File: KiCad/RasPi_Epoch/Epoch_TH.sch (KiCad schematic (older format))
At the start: 21 parts, among them P1 RasPi_GPIO, P2 CONN_1, P3 CONN_1, P4 CONN_1, P5 32k, P6 CONN_1, P7 CONN_1, P8 CONN_1, P9 SQW, U1 DS3231N, U2 DS1307, X1 CRYSTAL

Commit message: Epoch_smd looks done (all parts on lower side). Epoch_TH in progress.
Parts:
- removed C1: 100n, cnp_3mm_disc, symbol C
- removed P2, P3, P4: CONN_1, Pad01, symbol CONN_1
- removed P5: 32k, symbol CONN_2
- removed R4, R5: 4k7, rc03_vert, symbol R
- removed U1: DS3231N, DS3231, symbol DS3231N
- P9: footprint (none) -> ShortLink3
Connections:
- net labels removed: 32k, RST, Rpi_32k
- wire segments 78 -> 47
- no-connect marks 22 -> 23
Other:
- note removed: "Breakout Pads"
- moved on the sheet: R1, R2, R3

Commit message: RasPi_Epoch : Epoch_TH done. Need to verify the circuit and layout.
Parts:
- removed R1, R2, R3: 4k7, rc03_vert, symbol R
- added P2: I/O, Pad01, symbol I/O
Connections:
- wire segments 47 -> 41
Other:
- note added: "DS1307 (Optional)\nVcc is tied to 5V0 on Ras-Pi, but SCL and SDA are forced to 3V3\nsince no pull up resistors are used.\nNeed to verify if this works."
- note removed: "DS1307 (Optional)\nVcc is tied to 5V0 on Ras-Pi, but SCL and SDA are pulled up to 3V3.\nNeed to verify if this works."
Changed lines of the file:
@@
-EESchema Schematic File Version 2  date Friday 15 March 2013 09:54:40 PM IST
+EESchema Schematic File Version 2  date Friday 15 March 2013 10:32:39 PM IST
 LIBS:RasPi_RTC
 LIBS:RasPi_RTC2
@@
 Comment4 ""
 $EndDescr
+Wire Wire Line
+	4000 5650 5475 5650
+Wire Wire Line
+	5475 5650 5475 5550
+Wire Notes Line
+	1025 7000 1025 3675
+Wire Notes Line
+	1025 7000 5850 7000
+Wire Notes Line
+	5850 7000 5850 3675
+Wire Notes Line
+	5850 3675 1025 3675
+Wire Wire Line
+	3150 1900 3675 1900
+Wire Wire Line
+	5925 3000 5425 3000
+Wire Wire Line
+	5425 3000 5425 2900
+Wire Wire Line
+	1850 3000 1150 3000
+Wire Wire Line
+	3150 2100 3800 2100
+Wire Wire Line
+	3800 2100 3800 1025
+Connection ~ 1725 6150
+Wire Wire Line
+	1725 6200 1725 4500
+Connection ~ 2100 4700
+Wire Wire Line
+	2100 6200 2100 4700
+Connection ~ 2350 6700
+Wire Wire Line
+	2350 6700 2350 6600
+Connection ~ 1725 4700
+Connection ~ 2500 6700
+Wire Wire Line
+	2500 6700 2500 5550
+Wire Wire Line
+	4950 5250 4000 5250
+Wire Wire Line
+	2500 5550 2650 5550
+Wire Wire Line
+	2800 5900 2950 5900
+Wire Wire Line
+	2800 5900 2800 5750
+Wire Wire Line
+	2800 5350 2800 5200
+Wire Wire Line
+	3100 5850 3025 5850
+Wire Wire Line
+	4075 5850 4075 4700
+Wire Wire Line
+	4075 5850 4000 5850
+Wire Wire Line
+	3025 5850 3025 6825
+Wire Wire Line
+	3100 5250 3025 5250
+Connection ~ 3025 6700
+Wire Wire Line
+	3025 5250 3025 4475
+Connection ~ 3025 4575
+Wire Wire Line
+	4000 5450 4950 5450
+Wire Wire Line
+	4075 4700 1725 4700
+Wire Wire Line
+	2950 5450 2950 5200
+Wire Wire Line
+	2950 5450 3100 5450
+Wire Wire Line
+	3100 5650 2950 5650
+Wire Wire Line
+	2950 5650 2950 5900
+Wire Wire Line
+	2950 5200 2800 5200
+Wire Wire Line
+	2350 6200 2350 4575
+Wire Wire Line
+	2100 6600 2100 6700
+Connection ~ 2100 6700
+Wire Wire Line
+	1725 6650 1725 6700
+Connection ~ 1600 1900
+Wire Wire Line
+	1150 2100 1850 2100
+Wire Wire Line
+	1150 2000 1850 2000
+Wire Wire Line
+	1150 1900 1850 1900
+Wire Wire Line
+	2350 4575 3025 4575
+Wire Wire Line
+	1725 6700 3025 6700
+Wire Wire Line
+	1600 1025 1600 1900
+Wire Wire Line
+	5225 2900 5225 3000
+Wire Wire Line
+	5225 3000 4750 3000
+Wire Notes Line
+	10875 3675 6100 3675
+Wire Notes Line
+	10875 3675 10875 7000
+Wire Notes Line
+	10875 7000 6100 7000
+Wire Notes Line
+	6100 7000 6100 3675
+$Comp
+L I/O P2
+U 1 1 5143534F
+P 5475 5400
+F 0 "P2" V 5525 5400 40  0000 L CNN
+F 1 "I/O" H 5475 5455 30  0001 C CNN
+F 2 "Pad01" H 5475 5400 60  0001 C CNN
+	1    5475 5400
+	0    -1   -1   0
+$EndComp
 NoConn ~ 3150 3000
-Connection ~ 4400 5650
-Wire Wire Line
-	4400 5175 4400 5650
-Wire Notes Line
-	6100 7000 6100 3675
-Wire Notes Line
-	6100 7000 10875 7000
-Wire Notes Line
-	10875 7000 10875 3675
-Wire Notes Line
-	10875 3675 6100 3675
-Connection ~ 4650 4575
-Wire Wire Line
-	4075 4575 4900 4575
-Wire Wire Line
-	4900 4575 4900 4675
-Wire Wire Line
-	4750 3000 5225 3000
-Wire Wire Line
-	5225 3000 5225 2900
-Wire Wire Line
-	1600 1025 1600 1900
-Wire Wire Line
-	3025 6700 1725 6700
-Connection ~ 4650 5450
-Wire Wire Line
-	4650 5175 4650 5450
-Wire Wire Line
-	3025 4575 2350 4575
-Wire Wire Line
-	1850 1900 1150 1900
-Wire Wire Line
-	1150 2000 1850 2000
-Wire Wire Line
-	1150 2100 1850 2100
-Connection ~ 1600 1900
-Wire Wire Line
-	1725 6700 1725 6650
-Connection ~ 2100 6700
-Wire Wire Line
-	2100 6600 2100 6700
-Wire Wire Line
-	2350 4575 2350 6200
-Wire Wire Line
-	2950 5200 2800 5200
-Wire Wire Line
-	2950 5650 2950 5900
-Wire Wire Line
-	2950 5650 3100 5650
-Wire Wire Line
-	3100 5450 2950 5450
-Wire Wire Line
-	2950 5450 2950 5200
-Wire Wire Line
-	1725 4700 4075 4700
-Wire Wire Line
-	4000 5450 5375 5450
-Connection ~ 3025 4575
-Wire Wire Line
-	3025 4475 3025 5250
-Connection ~ 3025 6700
-Wire Wire Line
-	3025 5250 3100 5250
-Wire Wire Line
-	3025 6825 3025 5850
-Wire Wire Line
-	4000 5650 5375 5650
-Wire Wire Line
-	4000 5850 4075 5850
-Wire Wire Line
-	4075 5850 4075 4700
-Wire Wire Line
-	3025 5850 3100 5850
-Wire Wire Line
-	2800 5200 2800 5350
-Wire Wire Line
-	2800 5750 2800 5900
-Wire Wire Line
-	2800 5900 2950 5900
-Wire Wire Line
-	2650 5550 2500 5550
-Wire Wire Line
-	5375 5250 4000 5250
-Wire Wire Line
-	2500 5550 2500 6700
-Connection ~ 2500 6700
-Connection ~ 1725 4700
-Wire Wire Line
-	2350 6700 2350 6600
-Connection ~ 2350 6700
-Wire Wire Line
-	2100 6200 2100 4700
-Connection ~ 2100 4700
-Wire Wire Line
-	1725 4500 1725 6200
-Connection ~ 1725 6150
-Wire Wire Line
-	4650 4675 4650 4575
-Wire Wire Line
-	4900 5175 4900 5250
-Connection ~ 4900 5250
-Wire Wire Line
-	3800 1025 3800 2100
-Wire Wire Line
-	3800 2100 3150 2100
-Wire Wire Line
-	1850 3000 1150 3000
-Wire Wire Line
-	5425 2900 5425 3000
-Wire Wire Line
-	5425 3000 5925 3000
-Wire Wire Line
-	3150 1900 3675 1900
-Wire Notes Line
-	5850 3675 1025 3675
-Wire Notes Line
-	5850 3675 5850 7000
-Wire Notes Line
-	5850 7000 1025 7000
-Wire Notes Line
-	1025 7000 1025 3675
-Wire Wire Line
-	4400 4675 4400 4575
-Connection ~ 4400 4575
 Text Notes 1075 3825 0    60   ~ 0
-DS1307 (Optional)\nVcc is tied to 5V0 on Ras-Pi, but SCL and SDA are pulled up to 3V3.\nNeed to verify if this works.
-Text Label 4075 4575 0    40   ~ 0
-Rpi_3V3
+DS1307 (Optional)\nVcc is tied to 5V0 on Ras-Pi, but SCL and SDA are forced to 3V3\nsince no pull up resistors are used.\nNeed to verify if this works.
 $Comp
 L +5V #PWR01
@@
 NoConn ~ 3150 2200
 $Comp
-L R R3
-U 1 1 5124BEE6
-P 4900 4925
-F 0 "R3" H 5000 5050 50  0000 C CNN
-F 1 "4k7" V 4900 4925 50  0000 C CNN
-F 2 "rc03_vert" H 4900 4925 60  0001 C CNN
-	1    4900 4925
-	1    0    0    -1
-$EndComp
-$Comp
-L R R1
-U 1 1 5124B652
-P 4400 4925
-F 0 "R1" H 4300 4800 50  0000 C CNN
-F 1 "4k7" V 4400 4925 50  0000 C CNN
-F 2 "rc03_vert" H 4400 4925 60  0001 C CNN
-	1    4400 4925
-	-1   0    0    1
-$EndComp
-$Comp
 L GND #PWR03
 U 1 1 5124B650
@@
 Text Label 1825 4700 0    40   ~ 0
 BAT
-Text Label 5375 5250 0    40   ~ 0
+Text Label 4950 5250 0    40   ~ 0
 Rpi_SCL
-Text Label 5375 5450 0    40   ~ 0
+Text Label 4950 5450 0    40   ~ 0
 Rpi_SDA
-Text Label 5375 5650 0    40   ~ 0
+Text Label 4950 5650 0    40   ~ 0
 SQW
 $Comp
@@
 	0    1    1    0
 $EndComp
-$Comp
-L R R2
-U 1 1 5124B1B5
-P 4650 4925
-F 0 "R2" H 4750 5050 50  0000 C CNN
-F 1 "4k7" V 4650 4925 50  0000 C CNN
-F 2 "rc03_vert" H 4650 4925 60  0001 C CNN
-	1    4650 4925
-	1    0    0    -1
-$EndComp
 NoConn ~ 1850 2300

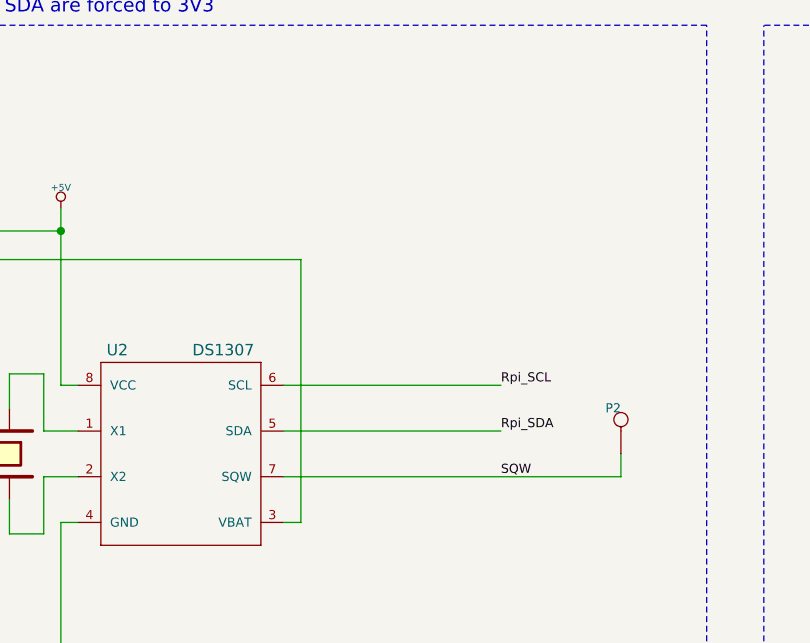
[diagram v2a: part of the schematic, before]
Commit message: RasPi_Epoch - Through Hole and SMD boards complete. Created seeed format BOM Files, Gerbers, some PDF's etc.
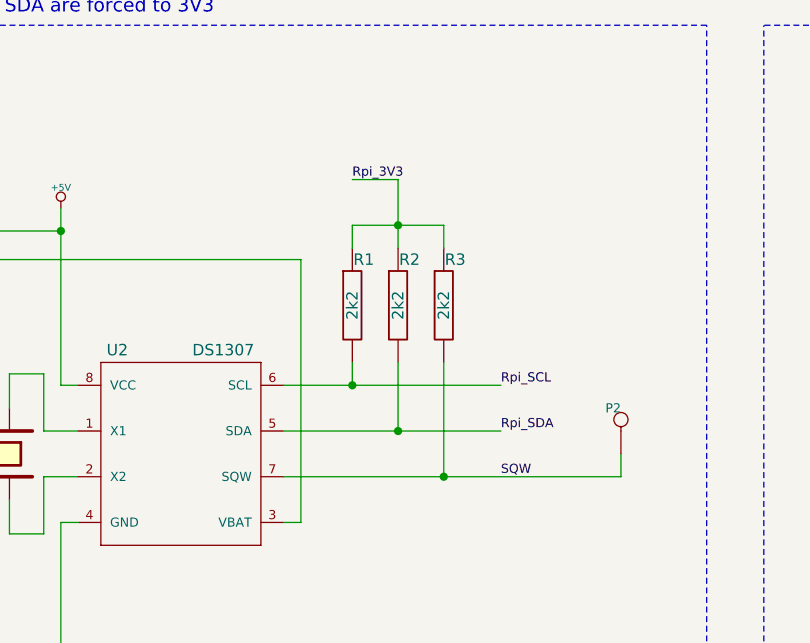
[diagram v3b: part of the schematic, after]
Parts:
- added R1, R2, R3: 2k2, rc03_vert, symbol R
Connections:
- wire segments 41 -> 49
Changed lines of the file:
@@
-EESchema Schematic File Version 2  date Friday 15 March 2013 10:32:39 PM IST
+EESchema Schematic File Version 2  date 18-Mar-13 12:42:11 PM
 LIBS:RasPi_RTC
 LIBS:RasPi_RTC2
@@
 encoding utf-8
 Sheet 1 1
-Title ""
-Date "15 mar 2013"
+Title "DS1307 based RTC for Raspberry-Pi"
+Date "16 mar 2013"
 Rev ""
-Comp ""
+Comp "www.wyolum.com"
 Comment1 ""
 Comment2 ""
@@
 Comment4 ""
 $EndDescr
+Text Label 4300 4350 0    40   ~ 0
+Rpi_3V3
+Wire Wire Line
+	4300 4350 4500 4350
+Wire Wire Line
+	4500 4350 4500 4650
+Wire Wire Line
+	4300 4650 4300 4550
+Wire Wire Line
+	4300 4550 4700 4550
+Wire Wire Line
+	4700 4550 4700 4650
+Connection ~ 4500 5450
+Wire Wire Line
+	4500 5150 4500 5450
 Wire Wire Line
 	4000 5650 5475 5650
@@
 Wire Notes Line
 	6100 7000 6100 3675
+Wire Wire Line
+	4300 5150 4300 5250
+Connection ~ 4300 5250
+Wire Wire Line
+	4700 5150 4700 5650
+Connection ~ 4700 5650
+Connection ~ 4500 4550
+$Comp
+L R R3
+U 1 1 51440D24
+P 4700 4900
+F 0 "R3" H 4750 5100 50  0000 C CNN
+F 1 "2k2" V 4700 4900 50  0000 C CNN
+F 2 "rc03_vert" V 4800 4900 50  0001 C CNN
+	1    4700 4900
+	1    0    0    -1
+$EndComp
+$Comp
+L R R2
+U 1 1 51440D20
+P 4500 4900
+F 0 "R2" H 4550 5100 50  0000 C CNN
+F 1 "2k2" V 4500 4900 50  0000 C CNN
+F 2 "rc03_vert" V 4600 4900 50  0001 C CNN
+	1    4500 4900
+	1    0    0    -1
+$EndComp
+$Comp
+L R R1
+U 1 1 51440D12
+P 4300 4900
+F 0 "R1" H 4350 5100 50  0000 C CNN
+F 1 "2k2" V 4300 4900 50  0000 C CNN
+F 2 "rc03_vert" V 4400 4900 50  0001 C CNN
+	1    4300 4900
+	1    0    0    -1
+$EndComp
 $Comp
 L I/O P2
